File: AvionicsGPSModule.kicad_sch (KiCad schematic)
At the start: 42 parts, among them P1 MC311D, Q1 AO3400A, Q2 AO3400A, U1 RP2040, U2 AP2112K-3.3, U3 L80-R, U4 W25Q128JVS, X1 ABM8-272-T3

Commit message: Added Marketing, fulfilled DRC, finalized board
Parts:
- C1, C10, C11, C12, C13, C14, C15, C2, C3, C4, C5, C6, C7, C8, C9: footprint Capacitor_SMD:C_0402_1005Metric -> Library:C_0402_1005Metric
- C17, C18, C19, C20, C21: footprint PCM_JLCPCB:C_0402 -> Library:C_0402_1005Metric
- P1: footprint MC-311D:USB-C-SMD_MC-311D -> Connector_USB:USB_C_Receptacle_GCT_USB4105-xx-A_16P_TopMnt_Horizontal
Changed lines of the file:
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@@
 			)
 		)
-		(property "Footprint" "Capacitor_SMD:C_0402_1005Metric"
+		(property "Footprint" "Library:C_0402_1005Metric"
 			(at 181.61 110.49 0)
 			(effects
@@
 			)
 		)
-		(property "Footprint" "Capacitor_SMD:C_0402_1005Metric"
+		(property "Footprint" "Library:C_0402_1005Metric"
 			(at 134.62 110.49 0)
 			(effects
@@
 			)
 		)
-		(property "Footprint" "Capacitor_SMD:C_0402_1005Metric"
+		(property "Footprint" "Library:C_0402_1005Metric"
 			(at 82.55 27.94 0)
 			(effects
@@
 			)
 		)
-		(property "Footprint" "Capacitor_SMD:C_0402_1005Metric"
+		(property "Footprint" "Library:C_0402_1005Metric"
 			(at 109.22 27.94 0)
 			(effects
@@
 			)
 		)
-		(property "Footprint" "PCM_JLCPCB:C_0402"
+		(property "Footprint" "Library:C_0402_1005Metric"
 			(at 173.482 73.66 90)
 			(effects
@@
 			)
 		)
-		(property "Footprint" "Capacitor_SMD:C_0402_1005Metric"
+		(property "Footprint" "Library:C_0402_1005Metric"
 			(at 189.23 135.89 0)
 			(effects
@@
 			)
 		)
-		(property "Footprint" "Capacitor_SMD:C_0402_1005Metric"
+		(property "Footprint" "Library:C_0402_1005Metric"
 			(at 115.57 123.19 0)
 			(effects
@@
 			)
 		)
-		(property "Footprint" "Capacitor_SMD:C_0402_1005Metric"
+		(property "Footprint" "Library:C_0402_1005Metric"
 			(at 163.83 110.49 0)
 			(effects
@@
 			)
 		)
-		(property "Footprint" "Capacitor_SMD:C_0402_1005Metric"
+		(property "Footprint" "Library:C_0402_1005Metric"
 			(at 157.48 135.89 0)
 			(effects
@@
 			)
 		)
-		(property "Footprint" "Capacitor_SMD:C_0402_1005Metric"
+		(property "Footprint" "Library:C_0402_1005Metric"
 			(at 143.51 110.49 0)
 			(effects
@@
 			)
 		)
-		(property "Footprint" "Capacitor_SMD:C_0402_1005Metric"
+		(property "Footprint" "Library:C_0402_1005Metric"
 			(at 115.57 132.08 0)
 			(effects
@@
 			)
 		)
-		(property "Footprint" "Capacitor_SMD:C_0402_1005Metric"
+		(property "Footprint" "Library:C_0402_1005Metric"
 			(at 125.73 110.49 0)
 			(effects
@@
 			)
 		)
-		(property "Footprint" "Capacitor_SMD:C_0402_1005Metric"
+		(property "Footprint" "Library:C_0402_1005Metric"
 			(at 190.5 110.49 0)
 			(effects
@@
 			)
 		)
-		(property "Footprint" "Capacitor_SMD:C_0402_1005Metric"
+		(property "Footprint" "Library:C_0402_1005Metric"
 			(at 153.67 110.49 0)
 			(effects
@@
 			)
 		)
-		(property "Footprint" "PCM_JLCPCB:C_0402"
+		(property "Footprint" "Library:C_0402_1005Metric"
 			(at 163.322 73.66 90)
 			(effects
@@
 			)
 		)
-		(property "Footprint" "MC-311D:USB-C-SMD_MC-311D"
+		(property "Footprint" "Connector_USB:USB_C_Receptacle_GCT_USB4105-xx-A_16P_TopMnt_Horizontal"
 			(at 29.21 49.53 0)
 			(effects
@@
 			)
 		)
-		(property "Footprint" "Capacitor_SMD:C_0402_1005Metric"
+		(property "Footprint" "Library:C_0402_1005Metric"
 			(at 115.57 142.24 0)
 			(effects
@@
 			)
 		)
-		(property "Footprint" "PCM_JLCPCB:C_0402"
+		(property "Footprint" "Library:C_0402_1005Metric"
 			(at 182.372 73.66 90)
 			(effects
@@
 			)
 		)
-		(property "Footprint" "PCM_JLCPCB:C_0402"
+		(property "Footprint" "Library:C_0402_1005Metric"
 			(at 154.432 73.66 90)
 			(effects
@@
 			)
 		)
-		(property "Footprint" "Capacitor_SMD:C_0402_1005Metric"
+		(property "Footprint" "Library:C_0402_1005Metric"
 			(at 173.99 110.49 0)
 			(effects
@@
 			)
 		)
-		(property "Footprint" "PCM_JLCPCB:C_0402"
+		(property "Footprint" "Library:C_0402_1005Metric"
 			(at 119.38 52.578 90)
 			(effects

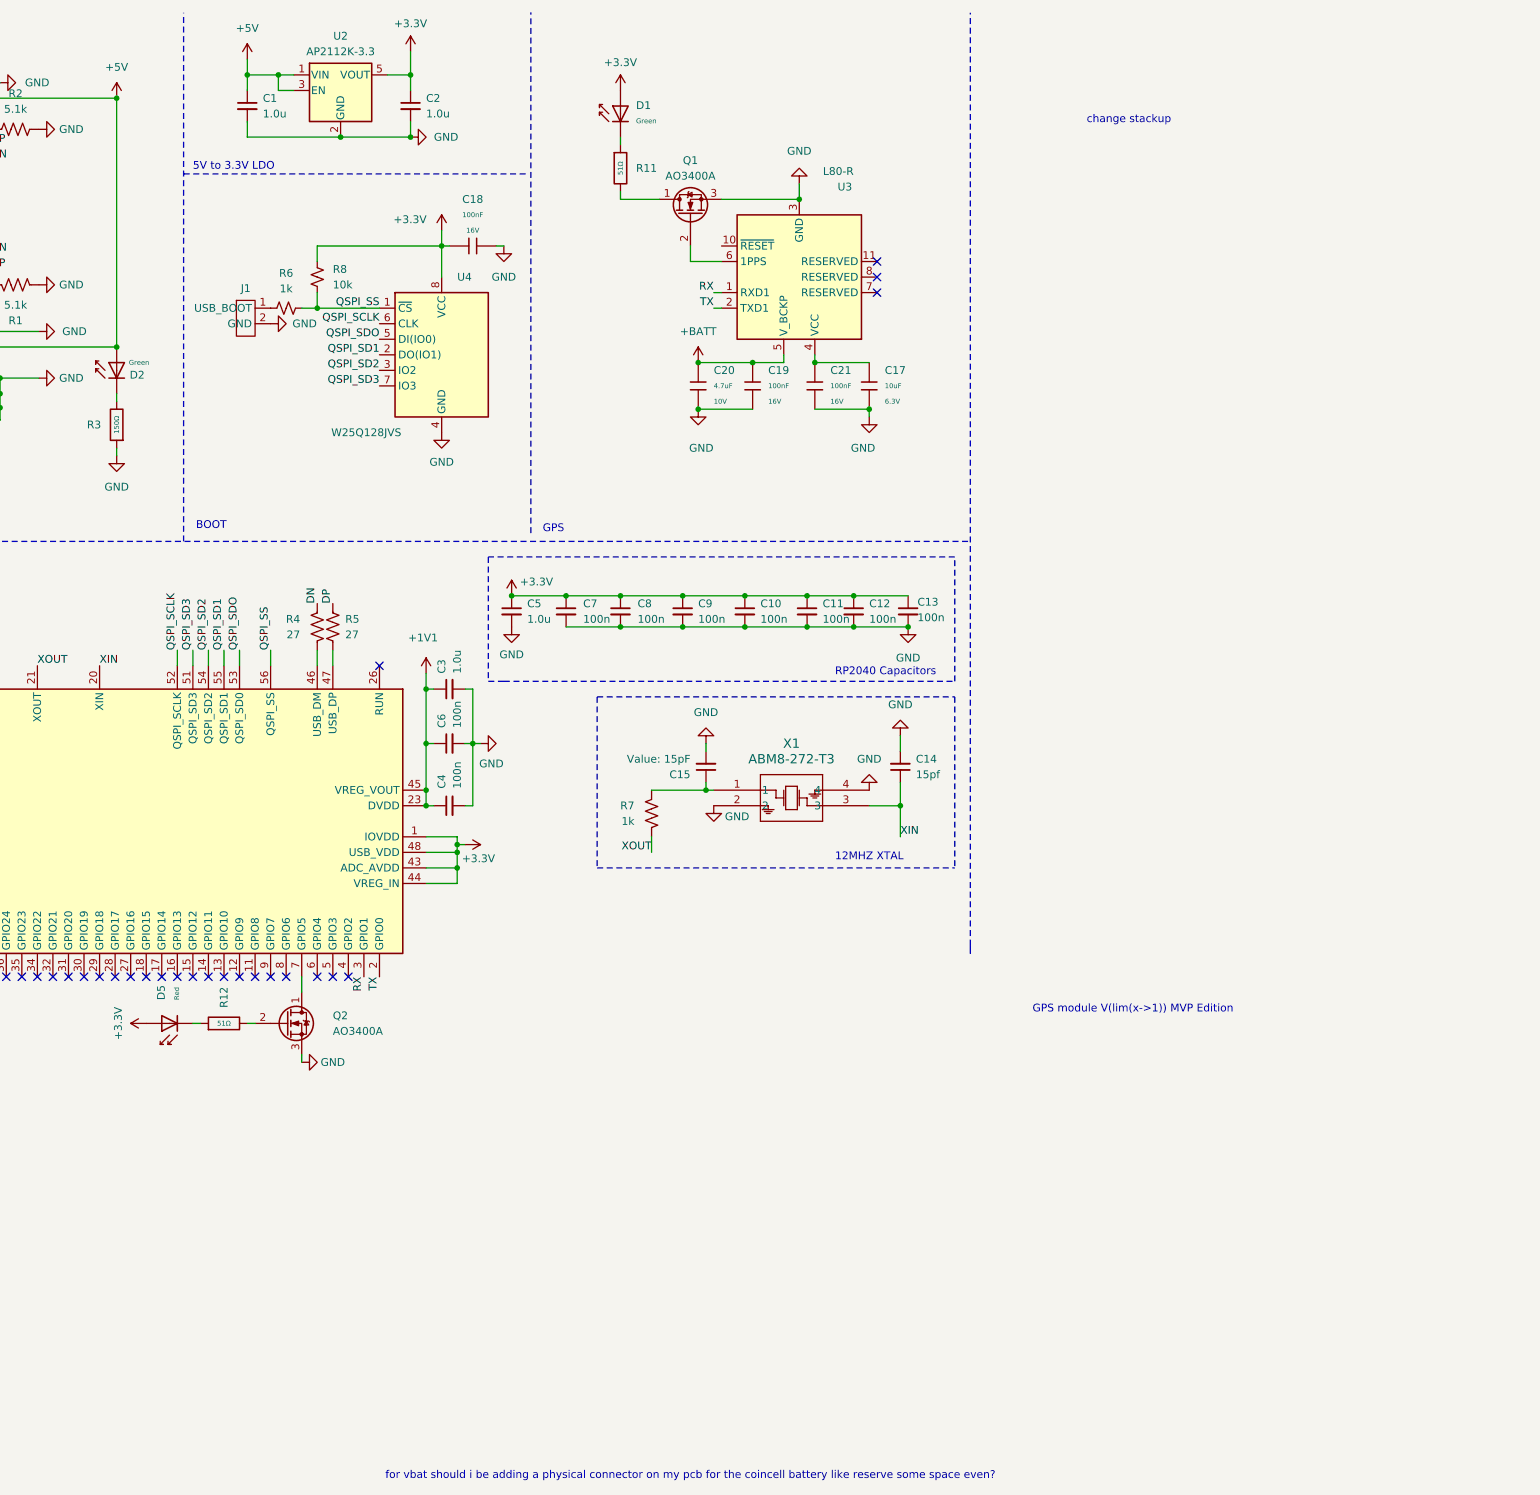
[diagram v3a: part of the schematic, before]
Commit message: added CAN Transciever
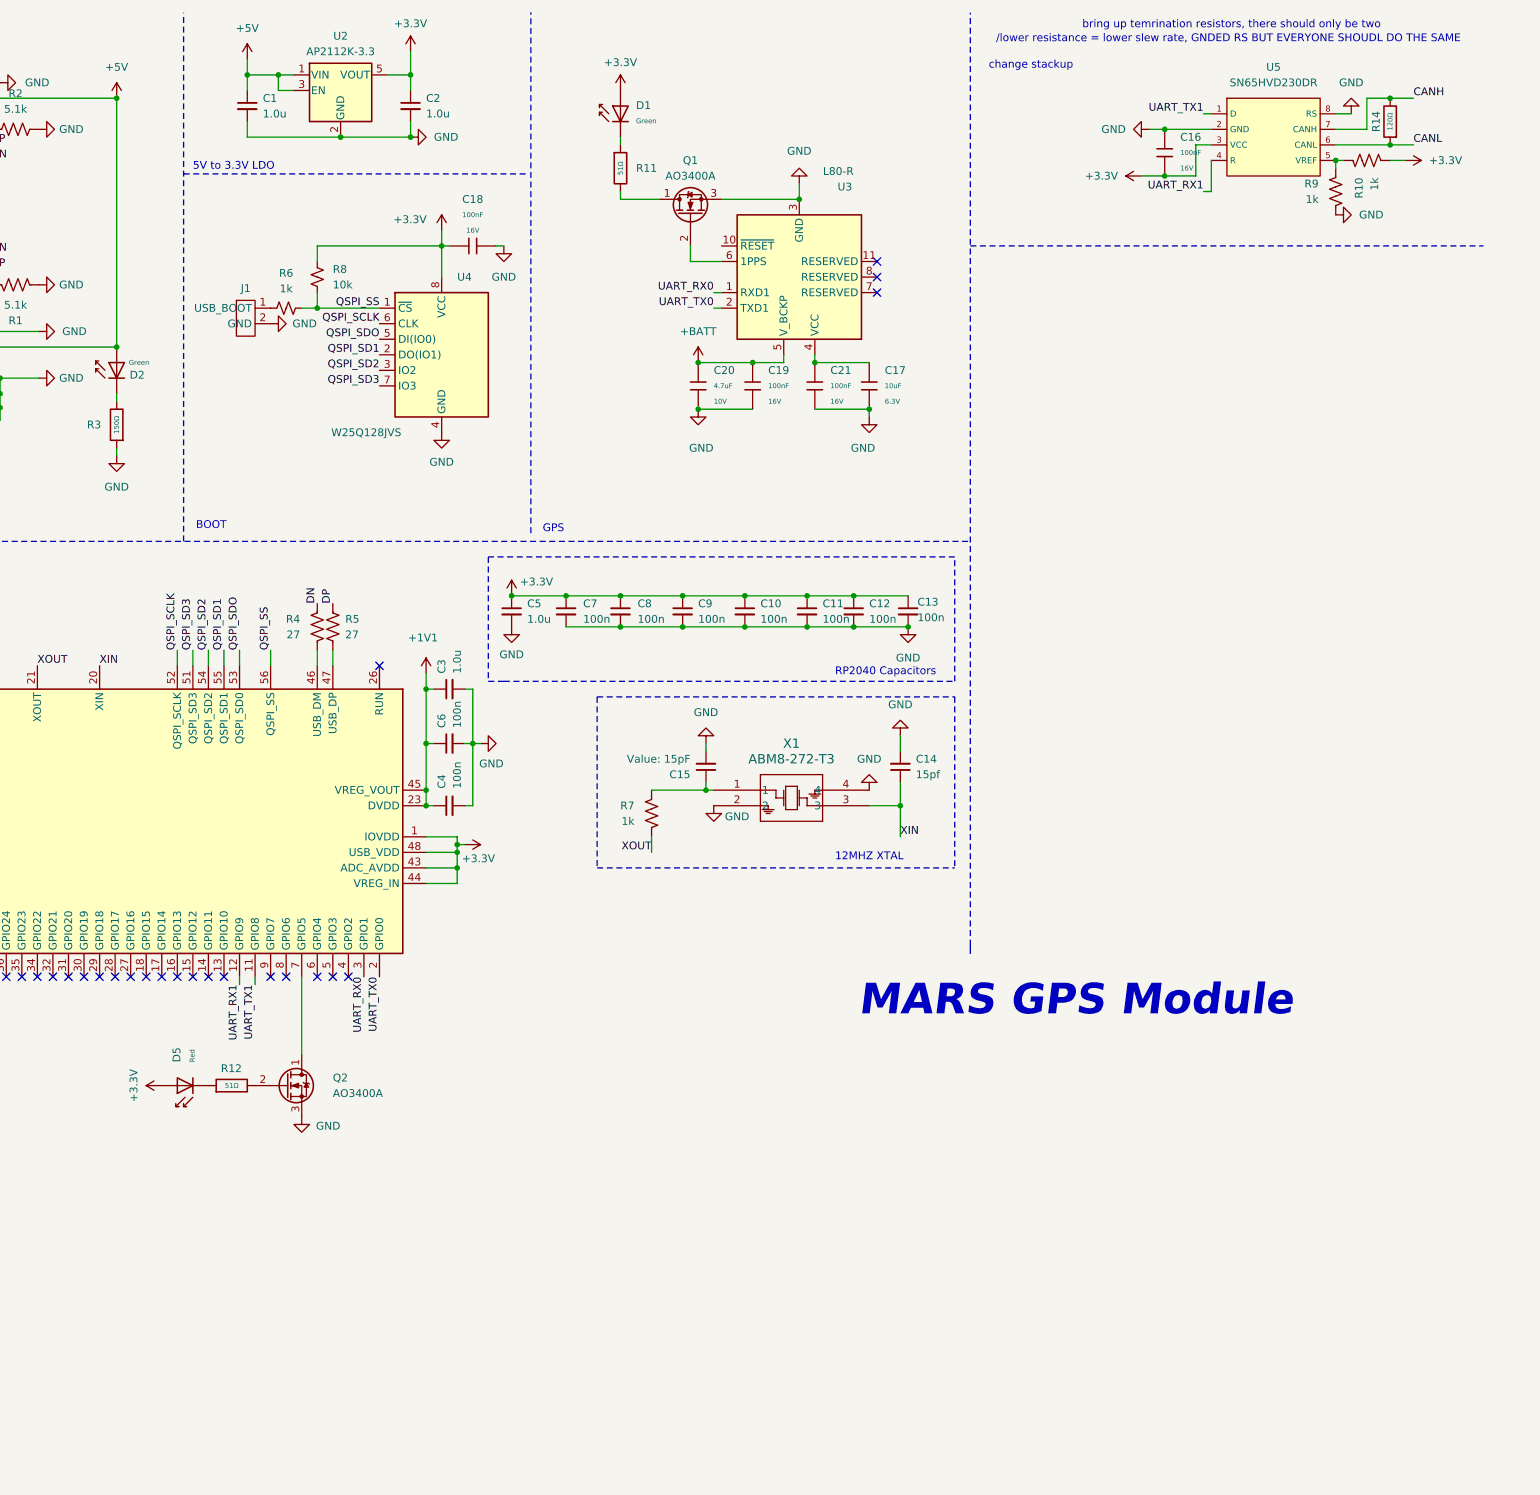
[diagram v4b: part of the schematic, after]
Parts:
- added C16: 100nF, PCM_JLCPCB:C_0402, symbol PCM_JLCPCB-Capacitors:0402,100nF
- added R10, R9: 1k, Resistor_SMD:R_0402_1005Metric, symbol Device:R_US
- added R14: 120Ω, PCM_JLCPCB:R_0402, symbol PCM_JLCPCB-Resistors:0402,120Ω
- added U5: SN65HVD230DR, PCM_JLCPCB:SOIC-8_L4.9-W3.9-P1.27-LS6.0-BL, symbol PCM_JLCPCB-Interface:Transceiver, CAN, SN65HVD230DR
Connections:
- net +3.3V: now also C16.2, R10.2, U5.3 (VCC)
- net GND: now also C16.1, R9.2, U5.2 (GND), U5.8 (RS)
- net UART_TX1: now reaches U1.11 (GPIO8)
- net UART_TX1: now also U5.1 (D)
- net UART_RX1: now reaches U1.12 (GPIO9)
- net UART_RX1: now also U5.4 (R)
- net RX renamed UART_RX0
- net TX renamed UART_TX0
- new net: R10.1, R9.1, U5.5 (VREF)
- new net CANH: R14.2, U5.7 (CANH)
- new net CANL: R14.1, U5.6 (CANL)
- no-connect marks 35 -> 33
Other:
- note added: "/lower resistance = lower slew rate, GNDED RS BUT EVERYONE SHOUDL DO THE SAME"
- note added: "MARS GPS Module"
- note added: "bring up temrination resistors, there should only be two"
- note removed: "GPS module V(lim(x->1)) MVP Edition"
- note removed: "for vbat should i be adding a physical connector on my pcb for the coincell battery like reserve some space even?"
- moved on the sheet: D5, Q2, R12

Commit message: Added CAN Transciever and CAN Controller
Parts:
- added C22, C23: 15pf, Library:C_0402_1005Metric, symbol Device:C_Small
- added C24: 100nF, PCM_JLCPCB:C_0402, symbol PCM_JLCPCB-Capacitors:0402,100nF
- added C25: 10nF, PCM_JLCPCB:C_0402, symbol PCM_JLCPCB-Capacitors:0402,10nF
- added R13: 5.1kΩ, PCM_JLCPCB:R_0402, symbol PCM_JLCPCB-Resistors:0402,5.1kΩ
- added U6: MCP2515_I/ML, Package_DFN_QFN:QFN-20-1EP_4x4mm_P0.5mm_EP2.5x2.5mm, symbol Interface_CAN_LIN:MCP2515-xST
- added X2: XTM32020000QT00351001, Crystal:Crystal_SMD_3225-4Pin_3.2x2.5mm, symbol Crystal:ABM8-272-T3
- C11: value 100n -> 1.0u
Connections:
- net +3.3V: now also C24.1, C25.1, R13.2, U6.20 (VDD)
- net GND: now also C22.2, C23.2, C24.2, C25.2, U6.10 (VSS), U6.3 (CLKOUT/SOF), X2.2, X2.4
- net at Q2.1 (D): now also U1.29 (GPIO18); no longer U1.7 (GPIO5)
- net SPI1 SCK: now reaches U1.13 (GPIO10)
- net SPI1 SCK: now also U6.14 (SCK)
- net SPI1 TX: now reaches U1.14 (GPIO11)
- net SPI1 TX: now also U6.16 (SI)
- net UART_RX0 renamed MCU_RX0
- net MCU_RX0: now also U3.2 (TXD1); no longer U3.1 (RXD1)
- net UART_RX1 renamed SPI1 CSn
- net SPI1 CSn: now also U6.18 (~{CS}); no longer U5.4 (R)
- net UART_TX0 renamed MCU_TX0
- net MCU_TX0: now also U3.1 (RXD1); no longer U3.2 (TXD1)
- net UART_TX1 renamed SPI1 RX
- net SPI1 RX: now also U6.17 (SO); no longer U5.1 (D)
- new net: R13.1, U6.19 (~{RESET})
- new net: C22.1, U6.8 (OSC2), X2.3
- new net: C23.1, U6.9 (OSC1), X2.1
- new net TRNS_RXD: U5.4 (R), U6.1 (TXCAN)
- new net TRNS_TXD: U5.1 (D), U6.2 (RXCAN)
- no-connect marks 33 -> 37
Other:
- note added: "CAN Transciever"
- note added: "NO LCSC PART"
- moved on the sheet: C16, D5, Q2, R12
